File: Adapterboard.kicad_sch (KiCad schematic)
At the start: 72 parts, among them J101 Conn_01x01_Pin, J102 Conn_01x01_Pin, J103 JTAG, J104 Conn_01x01_Pin, J105 TUNNEL_IN, J106 Power in +15V, J107 Power in -15V, J108 Power out Preamplifier, J109 Piezo, J110 TUNNEL_1, J111 USB_Connector, U102 DAC X, U103 ESP32-DEVKITC-32D, U104 DAC Y, U106 DAC Z, U107 ADC 8 Click, U108 mint, U109 UniRegensburg, U110 OTH, U201 TL072, U301 TL072

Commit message: complete for production
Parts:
- J101, J102, J104: footprint Connector_PinHeader_1.00mm:PinHeader_1x01_P1.00mm_Vertical -> Connector_PinHeader_2.54mm:PinHeader_1x01_P2.54mm_Vertical
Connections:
- net TUNNEL_GND: now also J105.1 (Pin_1); no longer J105.2 (Pin_2)
- net TUNNEL_IN: now also J105.2 (Pin_2); no longer J105.1 (Pin_1)
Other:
- moved on the sheet: J105
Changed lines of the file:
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@@
 	(wire
 		(pts
+			(xy 227.33 101.6) (xy 232.41 101.6)
+		)
+		(stroke
+			(width 0)
+			(type default)
+		)
+	)
+	(wire
+		(pts
 			(xy 33.02 54.61) (xy 40.64 54.61)
 		)
@@
 	(wire
 		(pts
-			(xy 227.33 99.06) (xy 242.57 99.06)
-		)
-		(stroke
-			(width 0)
-			(type default)
-		)
-	)
-	(wire
-		(pts
 			(xy 162.56 207.01) (xy 162.56 205.74)
 		)
@@
 		)
 	)
-	(polyline
+	(wire
 		(pts
-			(xy 287.02 26.67) (xy 318.77 26.67)
+			(xy 227.33 99.06) (xy 242.57 99.06)
 		)
 		(stroke
@@
 		)
 	)
-	(wire
+	(polyline
 		(pts
-			(xy 212.09 163.83) (xy 212.09 184.15)
+			(xy 287.02 26.67) (xy 318.77 26.67)
 		)
 		(stroke
@@
 	(wire
 		(pts
-			(xy 227.33 101.6) (xy 232.41 101.6)
+			(xy 212.09 163.83) (xy 212.09 184.15)
 		)
 		(stroke
@@
 			)
 		)
-		(property "Footprint" "Connector_PinHeader_1.00mm:PinHeader_1x01_P1.00mm_Vertical"
+		(property "Footprint" "Connector_PinHeader_2.54mm:PinHeader_1x01_P2.54mm_Vertical"
 			(at 109.22 105.41 0)
 			(effects
@@
 		(on_board yes)
 		(dnp no)
-		(fields_autoplaced yes)
 		(property "Reference" "J104"
 			(at 169.545 101.6 0)
@@
 		)
 		(property "Value" "Conn_01x01_Pin"
-			(at 169.545 104.14 0)
+			(at 170.18 104.14 0)
 			(effects
 				(font
@@
 			)
 		)
-		(property "Footprint" "Connector_PinHeader_1.00mm:PinHeader_1x01_P1.00mm_Vertical"
+		(property "Footprint" "Connector_PinHeader_2.54mm:PinHeader_1x01_P2.54mm_Vertical"
 			(at 168.91 106.68 0)
 			(effects
@@
 	(symbol
 		(lib_id "Connector:Screw_Terminal_01x02")
-		(at 222.25 99.06 0)
-		(mirror y)
+		(at 222.25 101.6 180)
 		(unit 1)
 		(exclude_from_sim no)
@@
 		(dnp no)
 		(property "Reference" "J105"
-			(at 223.52 96.52 0)
+			(at 223.52 104.14 0)
 			(effects
 				(font
@@
 		)
 		(property "Value" "TUNNEL_IN"
-			(at 229.235 105.41 0)
+			(at 229.235 95.25 0)
 			(effects
 				(font
@@
 		)
 		(property "Footprint" "TerminalBlock:TerminalBlock_Xinya_XY308-2.54-2P_1x02_P2.54mm_Horizontal"
-			(at 222.25 99.06 0)
+			(at 222.25 101.6 0)
 			(effects
 				(font
@@
 		)
 		(property "Datasheet" "~"
-			(at 222.25 99.06 0)
+			(at 222.25 101.6 0)
 			(effects
 				(font
@@
 		)
 		(property "Description" ""
-			(at 222.25 99.06 0)
+			(at 222.25 101.6 0)
 			(effects
 				(font
@@
 			)
 		)
-		(property "Footprint" "Connector_PinHeader_1.00mm:PinHeader_1x01_P1.00mm_Vertical"
+		(property "Footprint" "Connector_PinHeader_2.54mm:PinHeader_1x01_P2.54mm_Vertical"
 			(at 45.72 105.41 0)
 			(effects

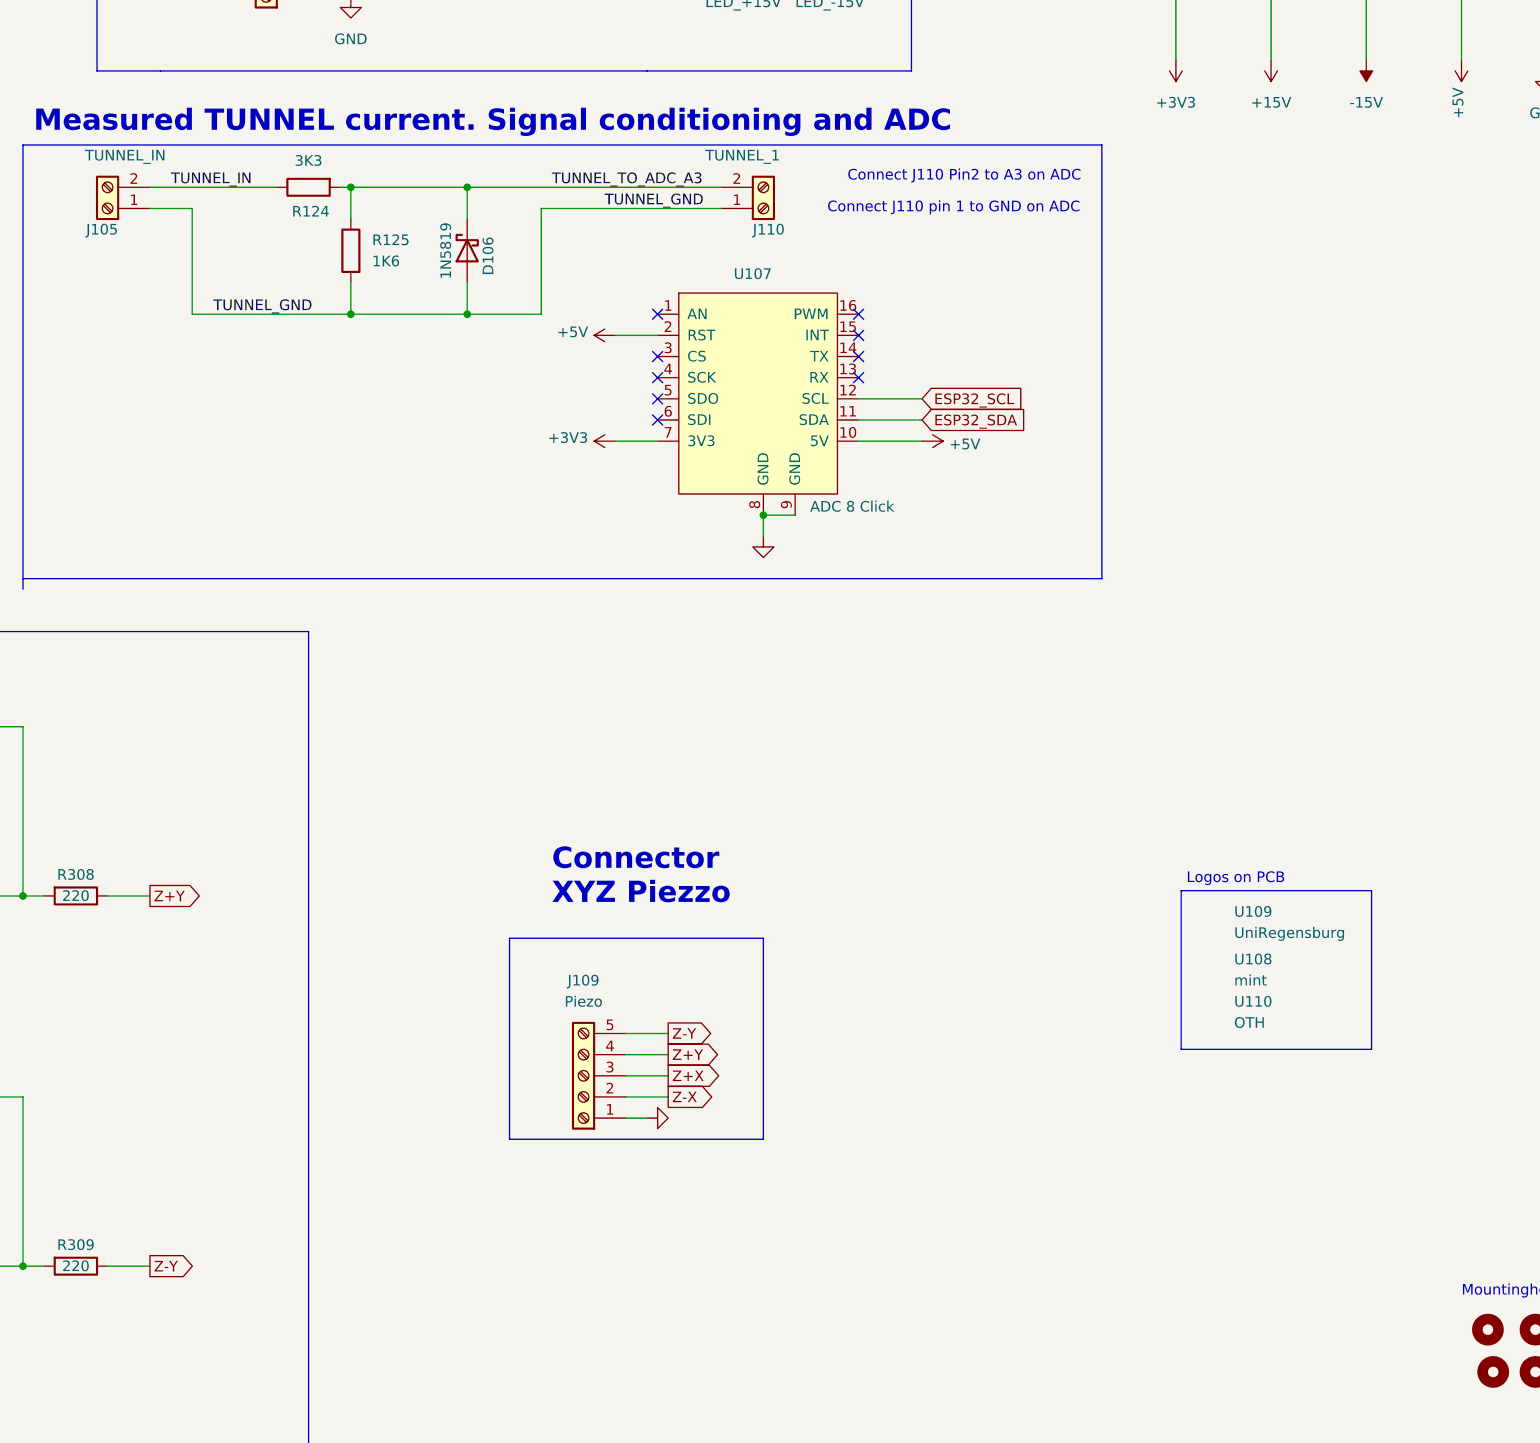
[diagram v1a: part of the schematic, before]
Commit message: ADS1115 added
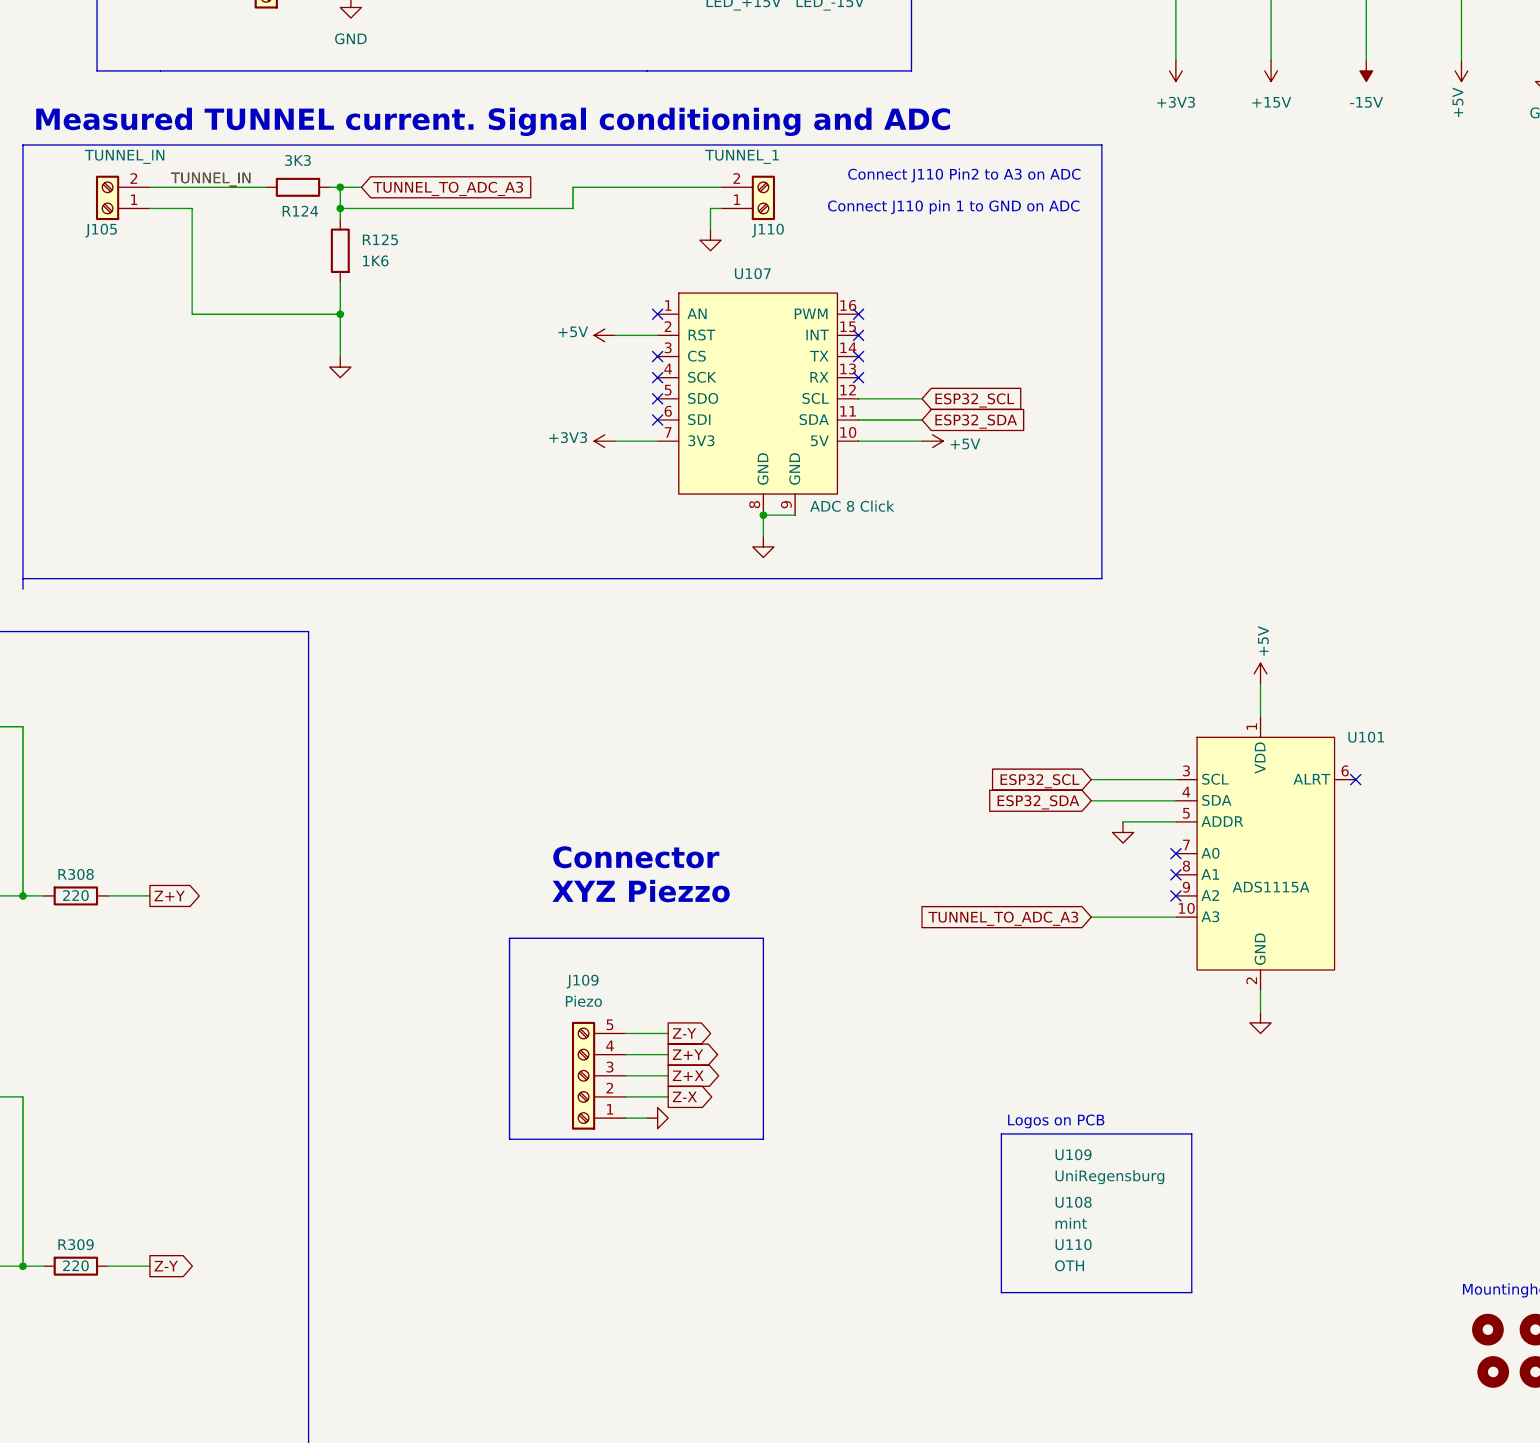
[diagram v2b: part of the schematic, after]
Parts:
- removed D106: 1N5819, Diode_THT:D_DO-41_SOD81_P10.16mm_Horizontal, symbol Diode:1N5819
- added U101: ADS1115A, Connector_PinHeader_2.54mm:PinHeader_1x10_P2.54mm_Vertical, symbol My_Library:ADS1115_ADC_module
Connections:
- net TUNNEL_GND is gone; now on net GND: J105.1 (Pin_1), J110.1 (Pin_1), R125.2
- net +5V: now also U101.1 (VDD)
- net ESP32_SCL: now also U101.3 (SCL)
- net ESP32_SDA: now also U101.4 (SDA)
- net GND: now also U101.2 (GND), U101.5 (ADDR)
- net TUNNEL_TO_ADC_A3: now also U101.10 (A3)
- no-connect marks 44 -> 48
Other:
- moved on the sheet: R124, R125
